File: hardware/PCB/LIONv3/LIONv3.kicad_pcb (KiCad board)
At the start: 2 copper layers, 45 x 75 mm, 67 parts, among them J1 CAN, J2 UART, J3 JTAG, J4 PWR_GND, J5 PWR_3.3V, J6 PWR_5V, J7 I2C, U1 TPS259474ARPWR, U10 XL-1608UBC-04, U11 XL-1608UBC-04, U12 TYPE-C_16PIN_2MD(073), U14 E80-900M2213S, U2 ESP32-C6-MINI-1-N4, U3 XL-1608UGC-04, U4 TLV75533PDQNR, U5 TCAN3414DR, U6 TMP112AIDRLR, U7 INA226AIDGSR, U8 XL-1608SURC-06, U9 INA226AIDGSR

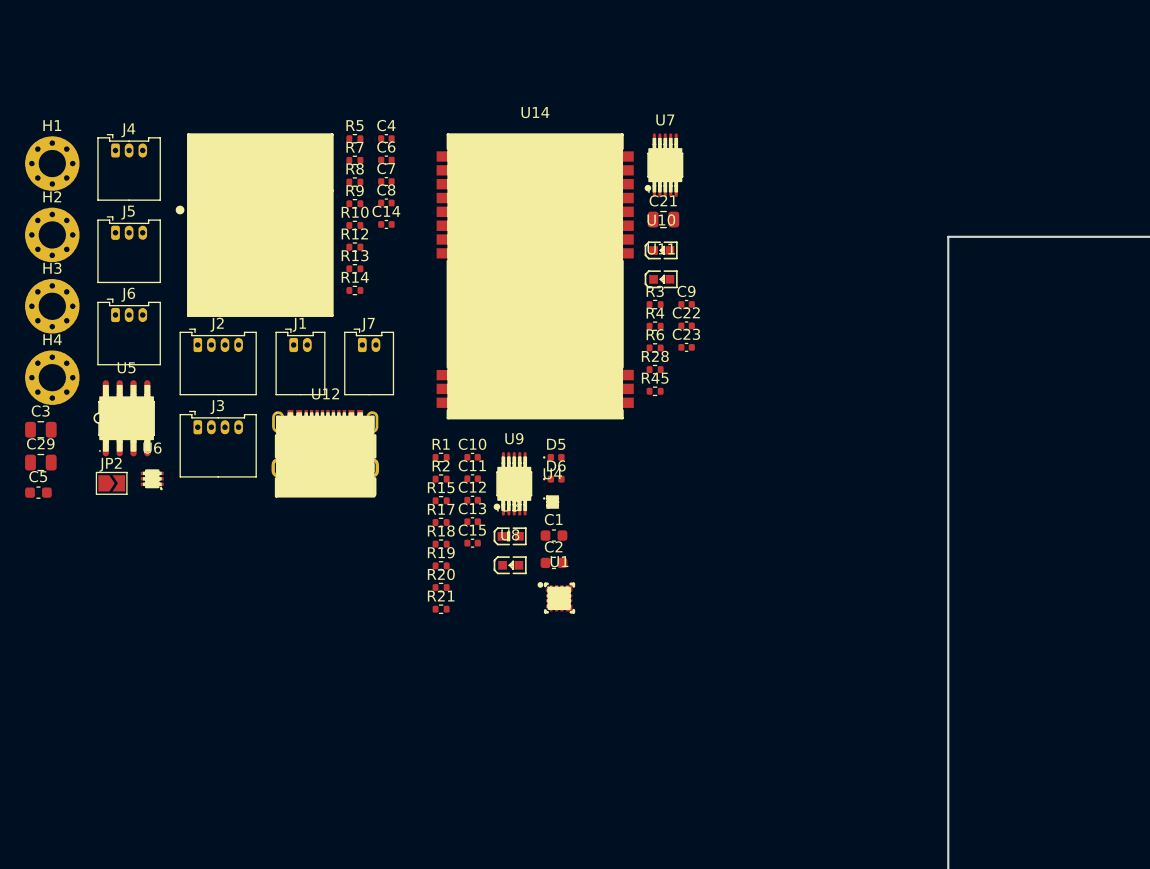
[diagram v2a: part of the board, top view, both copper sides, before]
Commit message: feat(hardware): add MOLEX connectors
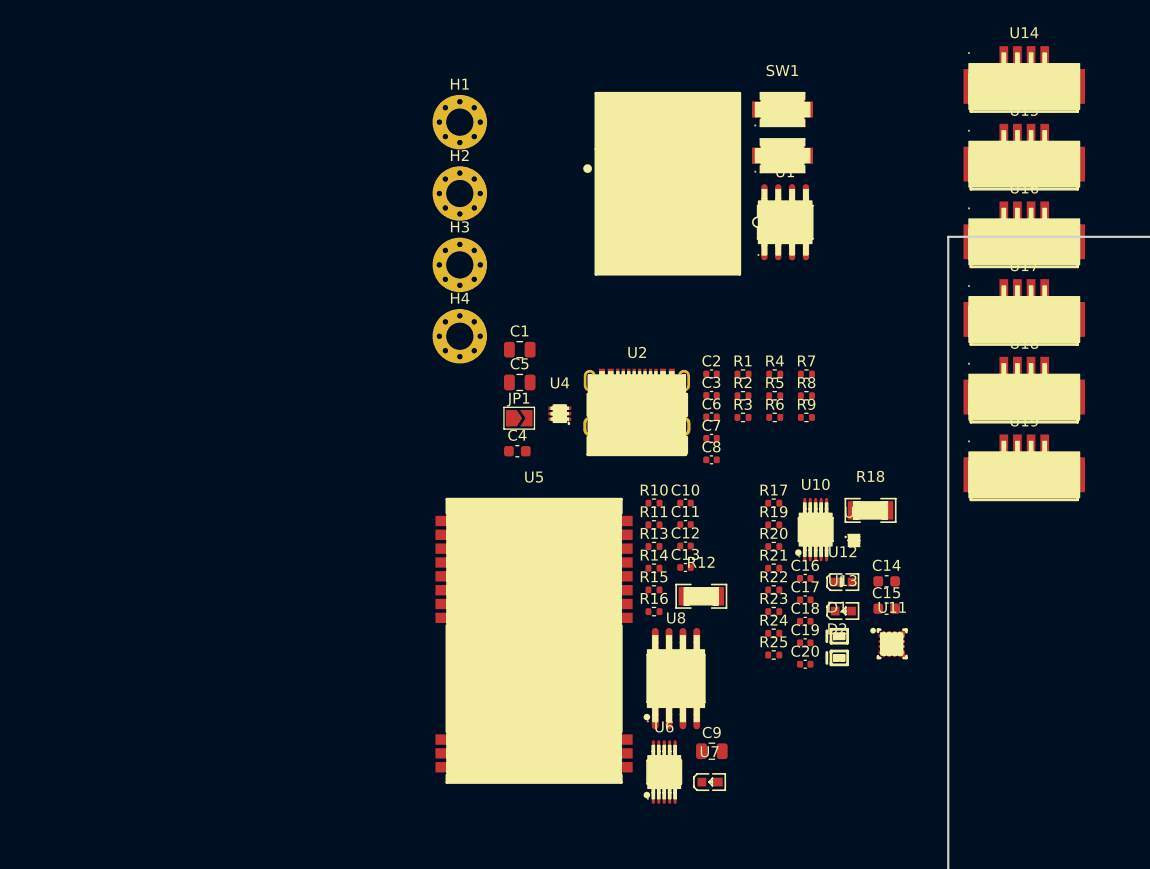
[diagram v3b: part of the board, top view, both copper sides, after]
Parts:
- removed C21: 22uF, Capacitor_SMD:C_0805_2012Metric
- removed C22, C23: 100nF, Capacitor_SMD:C_0402_1005Metric
- removed C29: 10uF, Capacitor_SMD:C_0805_2012Metric
- removed D5, D6: D_Schottky, Diode_SMD:D_0402_1005Metric
- removed J1: CAN, Connector_Molex:Molex_PicoBlade_53048-0210_1x02_P1.25mm_Horizontal
- removed J2: UART, Connector_Molex:Molex_PicoBlade_53048-0410_1x04_P1.25mm_Horizontal
- removed J3: JTAG, Connector_Molex:Molex_PicoBlade_53048-0410_1x04_P1.25mm_Horizontal
- removed J4: PWR_GND, Connector_Molex:Molex_PicoBlade_53048-0310_1x03_P1.25mm_Horizontal
- removed J5: PWR_3.3V, Connector_Molex:Molex_PicoBlade_53048-0310_1x03_P1.25mm_Horizontal
- removed J6: PWR_5V, Connector_Molex:Molex_PicoBlade_53048-0310_1x03_P1.25mm_Horizontal
- removed J7: I2C, Connector_Molex:Molex_PicoBlade_53048-0210_1x02_P1.25mm_Horizontal
- removed JP2: Jumper_2_Open, Jumper:SolderJumper-2_P1.3mm_Open_TrianglePad1.0x1.5mm
- removed R28, R45: 10k, Resistor_SMD:R_0402_1005Metric
- added C16: 100nF, Capacitor_SMD:C_0402_1005Metric, F.Cu at (138.1, 96.2)
- added C17: 1uF, Capacitor_SMD:C_0402_1005Metric, F.Cu at (138.1, 98.2)
- added C18: 3.3nF, Capacitor_SMD:C_0402_1005Metric, F.Cu at (138.1, 100.2)
- added C19: 2.2nF, Capacitor_SMD:C_0402_1005Metric, F.Cu at (138.1, 102.2)
- added C20: 1uF, Capacitor_SMD:C_0402_1005Metric, F.Cu at (138.1, 104.1)
- added D1: D_Schottky, LIONv3-Footprints:X2-DFN1006-2_L1.0-W0.6-P0.65-RD, F.Cu at (141.2, 101.6)
- added D2: D_Schottky, LIONv3-Footprints:X2-DFN1006-2_L1.0-W0.6-P0.65-RD, F.Cu at (141.2, 103.5)
- added JP1: Jumper_2_Open, Jumper:SolderJumper-2_P1.3mm_Open_TrianglePad1.0x1.5mm, F.Cu at (111.8, 81.5)
- added R11: 10k, Resistor_SMD:R_0402_1005Metric, F.Cu at (124.2, 91.3)
- added R16: 10k, Resistor_SMD:R_0402_1005Metric, F.Cu at (124.2, 99.3)
- added R22: 15k, Resistor_SMD:R_0402_1005Metric, F.Cu at (135.2, 97.3)
- added R23: 10k, Resistor_SMD:R_0402_1005Metric, F.Cu at (135.2, 99.3)
- added R24: 82, Resistor_SMD:R_0402_1005Metric, F.Cu at (135.2, 101.3)
- added R25: 150, Resistor_SMD:R_0402_1005Metric, F.Cu at (135.2, 103.3)
- added SW1: RESET, LIONv3-Footprints:KEY-SMD_L3.9-W3.0-LS5.0, F.Cu at (136.0, 53.2)
- added SW2: BOOT, LIONv3-Footprints:KEY-SMD_L3.9-W3.0-LS5.0, F.Cu at (136.0, 57.5)
- added U13: XL-1608SURC-06, LIONv3-Footprints:LED0603-RD_RED, F.Cu at (141.6, 99.2)
- added U15: UART, LIONv3-Footprints:CONN-SMD_4P-P1.25_53261-0471, F.Cu at (158.2, 56.8)
- added U16: UART, LIONv3-Footprints:CONN-SMD_4P-P1.25_53261-0471, F.Cu at (158.2, 63.9)
- added U17: UART, LIONv3-Footprints:CONN-SMD_4P-P1.25_53261-0471, F.Cu at (158.2, 71.0)
- added U18: UART, LIONv3-Footprints:CONN-SMD_4P-P1.25_53261-0471, F.Cu at (158.2, 78.2)
- added U19: UART, LIONv3-Footprints:CONN-SMD_4P-P1.25_53261-0471, F.Cu at (158.2, 85.3)
- C1: value 1uF -> 10uF; footprint Capacitor_SMD:C_0603_1608Metric -> Capacitor_SMD:C_0805_2012Metric
- C11: value 1uF -> 100nF
- C12: value 3.3nF -> 100nF
- C13: value 2.2nF -> 100nF
- C14, C4: value 100nF -> 1uF; footprint Capacitor_SMD:C_0402_1005Metric -> Capacitor_SMD:C_0603_1608Metric
- C15: footprint Capacitor_SMD:C_0402_1005Metric -> Capacitor_SMD:C_0603_1608Metric
- C2: value 1uF -> 100nF; footprint Capacitor_SMD:C_0603_1608Metric -> Capacitor_SMD:C_0402_1005Metric
- C3: value 22uF -> 100nF; footprint Capacitor_SMD:C_0805_2012Metric -> Capacitor_SMD:C_0402_1005Metric
- C5: value 1uF -> 22uF; footprint Capacitor_SMD:C_0603_1608Metric -> Capacitor_SMD:C_0805_2012Metric
- C6: value 100nF -> 4.7 nF
- C8: value 4.7 nF -> 100nF
- C9: value 100nF -> 22uF; footprint Capacitor_SMD:C_0402_1005Metric -> Capacitor_SMD:C_0805_2012Metric
- R1: value 150 -> 0
- R10: value 5.1k -> 10k
- R12: value 61 -> 50m; footprint Resistor_SMD:R_0402_1005Metric -> LIONv3-Footprints:R1206
- R13: value 61 -> 10k
- R14: value 4.7k -> 68
- R17: value 133k -> 10k
- R18: value 100k -> 50m; footprint Resistor_SMD:R_0402_1005Metric -> LIONv3-Footprints:R1206
- R19: value 6.65k -> 133k
- R2: value 82 -> 62
- R20: value 15k -> 100k
- R21: value 10k -> 6.65k
- R3: value 68 -> 62
- R4: value 68 -> 10k
- R5, R6: value 10k -> 5.1k
- R7: value 0 -> 10k
- R9: value 5.1k -> 4.7k
- U1: value TPS259474ARPWR -> TCAN3414DR; footprint LIONv3-Footprints:VQFN-10_L2.0-W2.0-P0.45-TL -> LIONv3-Footprints:SOIC-8_L4.9-W3.9-P1.27-LS6.0-BL
- U10: value XL-1608UBC-04 -> INA226AIDGSR; footprint LIONv3-Footprints:LED0603-RD_BLUE -> LIONv3-Footprints:MSOP-10_L3.0-W3.0-P0.50-LS5.0-BL
- U11: value XL-1608UBC-04 -> TPS259474ARPWR; footprint LIONv3-Footprints:LED0603-RD_BLUE -> LIONv3-Footprints:VQFN-10_L2.0-W2.0-P0.45-TL
- U12: value TYPE-C_16PIN_2MD(073) -> XL-1608UGC-04; footprint LIONv3-Footprints:USB-C-SMD_TYPE-C-16PIN-2MD-073 -> LIONv3-Footprints:LED0603-RD_GREEN
- U14: value E80-900M2213S -> UART; footprint LIONv3-Footprints:WIFIM-SMD_22P-L26.0-W16.0-P1.27-TL -> LIONv3-Footprints:CONN-SMD_4P-P1.25_53261-0471
- U2: value ESP32-C6-MINI-1-N4 -> TYPE-C_16PIN_2MD(073); footprint LIONv3-Footprints:WIFIM-SMD_61P-L16.6-W13.2-P0.80-ESP32-C6-MINI-1-N4 -> LIONv3-Footprints:USB-C-SMD_TYPE-C-16PIN-2MD-073
- U3: value XL-1608UGC-04 -> ESP32-C6-MINI-1-N4; footprint LIONv3-Footprints:LED0603-RD_GREEN -> LIONv3-Footprints:WIFIM-SMD_61P-L16.6-W13.2-P0.80-ESP32-C6-MINI-1-N4
- U4: value TLV75533PDQNR -> TMP112AIDRLR; footprint LIONv3-Footprints:X2SON-4_L1.0-W1.0-P0.65-TL-EP -> LIONv3-Footprints:SOT-563_L1.6-W1.2-P0.50-LS1.6-BR
- U5: value TCAN3414DR -> E80-900M2213S; footprint LIONv3-Footprints:SOIC-8_L4.9-W3.9-P1.27-LS6.0-BL -> LIONv3-Footprints:WIFIM-SMD_22P-L26.0-W16.0-P1.27-TL
- U6: value TMP112AIDRLR -> INA226AIDGSR; footprint LIONv3-Footprints:SOT-563_L1.6-W1.2-P0.50-LS1.6-BR -> LIONv3-Footprints:MSOP-10_L3.0-W3.0-P0.50-LS5.0-BL
- U7: value INA226AIDGSR -> XL-1608UBC-04; footprint LIONv3-Footprints:MSOP-10_L3.0-W3.0-P0.50-LS5.0-BL -> LIONv3-Footprints:LED0603-RD_BLUE
- U8: value XL-1608SURC-06 -> W25Q16JVSSIQTR; footprint LIONv3-Footprints:LED0603-RD_RED -> LIONv3-Footprints:SOIC-8_L5.3-W5.3-P1.27-LS8.0-BL
- U9: value INA226AIDGSR -> TLV75533PDQNR; footprint LIONv3-Footprints:MSOP-10_L3.0-W3.0-P0.50-LS5.0-BL -> LIONv3-Footprints:X2SON-4_L1.0-W1.0-P0.65-TL-EP
- moved C3 61.6 mm to (129.5, 79.5)
- moved U7 56.8 mm to (129.3, 114.9)
- moved C14 56.4 mm to (145.5, 96.5)
- moved U6 54.1 mm to (125.1, 114.0)
- moved U12 49.3 mm to (141.6, 96.6)
- moved U14 48.8 mm to (158.2, 49.7)
- moved R7 45.8 mm to (138.2, 77.5)
- moved R8 45.8 mm to (138.2, 79.5)
- moved R9 45.8 mm to (138.2, 81.5)
- moved C5 45.3 mm to (111.9, 78.3)
- moved R5 45.2 mm to (135.3, 79.5)
- moved R12 45.1 mm to (128.5, 97.9)
- moved U5 42.8 mm to (113.2, 102.3)
- moved C9 41.1 mm to (129.5, 112.1)
- moved U1 40.3 mm to (136.2, 63.6)
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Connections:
- C1 pad 1: Net-(D5-K) -> +3.3V
- C10 pad 1: Net-(U9-VS+) -> 3.3V_RF
- C11 pad 1: /POWER/3V3_IN -> /LR_RST
- C12 pad 1: Net-(U1-ITIMER) -> +3.3V
- C13 pad 1: Net-(U1-DVDT) -> +3.3V
- C14 pad 1: +3.3V -> Net-(D1-K)
- C15 pad 1: +3.3V -> /POWER/PWR
- C2 pad 1: /POWER/3V3_IN -> +3.3V
- C3 pad 1: +3V3 -> Net-(C3-Pad1)
- C4 pad 1: +3V3 -> Net-(U3-EN)
- C5 pad 1: Net-(U2-EN) -> +3.3V
- C6 pad 1: +3.3V -> Net-(C6-Pad1)
- C7 pad 1: Net-(C7-Pad1) -> +3.3V
- C8 pad 1: Net-(C8-Pad1) -> +3.3V
- C9 pad 1: +3.3V -> 3.3V_RF
- R1 pad 1: Net-(U8-A) -> Net-(C3-Pad1)
- R1 pad 2: /POWER/3V3_IN -> Net-(U3-EN)
- R10 pad 1: Net-(U12-CC2) -> 3.3V_RF
- R10 pad 2: GND -> /LR_NSS
- R12 pad 1: Net-(JP2-B) -> +3.3V
- R12 pad 2: Net-(C8-Pad1) -> 3.3V_RF
- R13 pad 1: Net-(C8-Pad1) -> +3.3V
- R13 pad 2: /CAN_A_N -> /FLASH_CS
- R14 pad 1: +3.3V -> Net-(U7-A)
- R14 pad 2: /TMP_ALERT -> /LR_LED
- R15 pad 1: /POWER/PWR_INA_ALERT -> +3.3V
- R15 pad 2: +3.3V -> Net-(U8-IO3)
- R17 pad 1: /POWER/3V3_IN -> /INA_ALERT
- R17 pad 2: Net-(U1-EN/UVLO) -> +3.3V
- R18 pad 1: Net-(U1-EN/UVLO) -> /POWER/PWR
- R18 pad 2: GND -> /POWER/3V3_IN
- R19 pad 1: Net-(U1-ILM) -> /POWER/3V3_IN
- R19 pad 2: GND -> Net-(U11-EN/UVLO)
- R2 pad 1: Net-(U3-A) -> Net-(JP1-B)
- R2 pad 2: +3.3V -> Net-(C6-Pad1)
- R20 pad 1: +3.3V -> Net-(U11-EN/UVLO)
- R20 pad 2: Net-(U1-FLT#/PGTH) -> GND
- R21 pad 1: Net-(U1-FLT#/PGTH) -> Net-(U11-ILM)
- R3 pad 1: Net-(U10-A) -> Net-(C6-Pad1)
- R3 pad 2: /LR_LED_TX -> /CAN_A_N
- R4 pad 1: Net-(U11-A) -> +3.3V
- R4 pad 2: /LR_LED_RX -> Net-(U3-EN)
- R5 pad 1: +3V3 -> Net-(U2-CC1)
- R5 pad 2: Net-(U2-EN) -> GND
- R6 pad 1: /INA_ALERT -> Net-(U2-CC2)
- R6 pad 2: +3.3V -> GND
- R7 pad 1: Net-(C7-Pad1) -> +3.3V
- R7 pad 2: Net-(U2-EN) -> /IO9
- R9 pad 1: Net-(U12-CC1) -> +3.3V
- R9 pad 2: GND -> /TMP_ALERT
- U1 pad 1: Net-(U1-EN/UVLO) -> /CAN_TX
- U1 pad 3: /POWER/LED_FAULT -> +3.3V
- U1 pad 4: Net-(U1-FLT#/PGTH) -> /CAN_RX
- U1 pad 5: /POWER/3V3_IN -> GND
- U1 pad 6: +3.3V -> /CAN_A_N
- U1 pad 7: Net-(U1-DVDT) -> /CAN_A_P
- U1 pad 8: GND -> /CAN_STB
- U10 pad 2: Net-(U10-A) -> /I2C_SDA
- U11 pad 1: GND -> Net-(U11-EN/UVLO)
- U11 pad 2: Net-(U11-A) -> GND
- U14 pad 1: GND -> +3.3V
- U14 pad 2: unconnected-(U14-NC-Pad2) -> /UART_TX0
- U14 pad 3: /SPI_MISO -> /UART_RX0
- U14 pad 4: /SPI_MOSI -> GND
- U14 pad 5: /SPI_SCK -> GND
- U14 pad 6: /LR_NSS -> GND
- U2 pad 13: unconnected-(U2-IO1-Pad13) -> GND
- U3 pad 2: Net-(U3-A) -> GND
- U4 pad 1: /POWER/3V3_IN -> /I2C_SCL
- U4 pad 3: Net-(D5-K) -> /TMP_ALERT
- U4 pad 4: Net-(D5-K) -> GND
- U4 pad 5: GND -> +3.3V
- U5 pad 1: /CAN1_TX -> GND
- U5 pad 2: GND -> unconnected-(U5-NC-Pad2)
- U5 pad 3: +3.3V -> /SPI_MISO
- U5 pad 4: /CAN1_RX -> /SPI_MOSI
- U5 pad 5: GND -> /SPI_SCK
- U5 pad 6: /CAN_A_N -> /LR_NSS
- U5 pad 7: /CAN_A_P -> /LR_BUSY
- U5 pad 8: /CAN1_STB -> GND
- U6 pad 1: /SCL -> GND
- U6 pad 3: /TMP_ALERT -> unconnected-(U6-Alert-Pad3)
- U6 pad 4: GND -> /I2C_SDA
- U6 pad 5: +3.3V -> /I2C_SCL
- U6 pad 6: /SDA -> +3.3V
- U7 pad 2: GND -> Net-(U7-A)
- U8 pad 1: /POWER/LED_FAULT -> /FLASH_CS
- U8 pad 2: Net-(U8-A) -> /SPI_MISO
- U9 pad 1: GND -> /POWER/PWR
- U9 pad 3: /POWER/PWR_INA_ALERT -> Net-(D1-K)
- U9 pad 4: /POWER/I2C1_SDA -> Net-(D1-K)
- U9 pad 5: /POWER/I2C1_SCL -> GND

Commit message: feat(hardware): finish board schematic
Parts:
- removed D2: D_Schottky, LIONv3-Footprints:X2-DFN1006-2_L1.0-W0.6-P0.65-RD
- removed U9: TLV75533PDQNR, LIONv3-Footprints:X2SON-4_L1.0-W1.0-P0.65-TL-EP
- added C21: 2.2uF, Capacitor_SMD:C_0603_1608Metric, F.Cu at (130.8, 130.0)
- added C22: 2.2uF, Capacitor_SMD:C_0603_1608Metric, F.Cu at (130.8, 132.5)
- added D3: D_Schottky, LIONv3-Footprints:X2-DFN1006-2_L1.0-W0.6-P0.65-RD, F.Cu at (127.3, 130.0)
- added D4: D_Schottky, LIONv3-Footprints:X2-DFN1006-2_L1.0-W0.6-P0.65-RD, F.Cu at (127.3, 132.5)
- added R26: 4.7k, Resistor_SMD:R_0402_1005Metric, F.Cu at (136.4, 129.7)
- added R27: 4.7k, Resistor_SMD:R_0402_1005Metric, F.Cu at (136.4, 131.7)
- added R28: 0, Resistor_SMD:R_0402_1005Metric, F.Cu at (136.4, 133.7)
- added R29: 0, Resistor_SMD:R_0402_1005Metric, F.Cu at (136.4, 135.7)
- added R30: 20k, Resistor_SMD:R_0402_1005Metric, F.Cu at (127.0, 134.7)
- added R31: 10k, Resistor_SMD:R_0402_1005Metric, F.Cu at (127.0, 136.7)
- added U20: TLV76733DRVR, LIONv3-Footprints:WSON-6_L2.0-W2.0-P0.65-TL-EP, F.Cu at (131.1, 135.4)
- C14, C15: value 1uF -> TBD; footprint Capacitor_SMD:C_0603_1608Metric -> Capacitor_SMD:C_0402_1005Metric
- C6: value 4.7 nF -> 4.7nF
- D1: value D_Schottky -> TI ESD752DBZR; footprint LIONv3-Footprints:X2-DFN1006-2_L1.0-W0.6-P0.65-RD -> Package_TO_SOT_SMD:SOT-23-3
- R2, R3: value 62 -> 59
- R21: value 6.65k -> 3.32k
- U14, U2: moved to B.Cu
- U15: value UART -> I2C; moved to B.Cu
- U16: value UART -> CAN; moved to B.Cu
- U17: value UART -> PWR_3V3; moved to B.Cu
- U18: value UART -> PWR_5V; moved to B.Cu
- U19: value UART -> PWR_GND; moved to B.Cu
- moved H1 94.5 mm to (193.3, 91.4)
- moved H2 87.1 mm to (193.2, 68.2)
- moved U2 70.2 mm to (192.7, 76.4), turned to -90 degrees
- moved U6 68.3 mm to (189.5, 91.2), turned to 90 degrees
- moved U3 64.5 mm to (189.4, 71.5)
- moved U8 54.8 mm to (178.8, 90.2), turned to 90 degrees
- moved U5 54.4 mm to (162.8, 80.0)
- moved U1 52.6 mm to (185.7, 81.4)
- moved SW2 52.0 mm to (179.6, 85.8)
- moved U14 51.4 mm to (192.2, 88.2), turned to -90 degrees
- moved H4 50.9 mm to (154.7, 90.0)
- moved SW1 49.9 mm to (177.4, 81.0)
- moved H3 48.1 mm to (154.5, 68.7)
- moved U10 41.4 mm to (177.1, 75.6), turned to 90 degrees
- moved U15 31.4 mm to (187.2, 68.8)
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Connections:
- C14 pad 1: Net-(D1-K) -> /USB_D+
- C15 pad 1: /POWER/PWR -> /USB_D-
- C16 pad 1: +3.3V -> /POWER/PWR
- D1 pad 1: Net-(D1-K) -> /CAN_STB
- D1 pad 2: +5V -> /CAN_A_N
- R17 pad 2: +3.3V -> /POWER/PWR
- U10 pad 6: +3.3V -> /POWER/PWR
- U11 pad 2: GND -> Net-(U11-OVLO/OVCSEL)
- U3 pad 17: /USB_D- -> Net-(U3-IO12)
- U3 pad 18: /USB_D+ -> Net-(U3-IO13)
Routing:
- net (no net): vias 0 -> 55

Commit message: feat(hardware): add TPS259474ARPWR PCB circuit
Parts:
- removed R30: 20k, Resistor_SMD:R_0402_1005Metric
- removed R31: 10k, Resistor_SMD:R_0402_1005Metric
- added R32: 34.8k, Resistor_SMD:R_0402_1005Metric, F.Cu at (176.4, 88.0)
- R19: value 133k -> 60.4k
- R20: value 100k -> 10k
- U14, U15, U16, U17, U18, U19, U2: moved to F.Cu
- moved JP1 284.4 mm to (381.4, 172.3)
- moved C1 281.6 mm to (370.6, 186.6)
- moved C2 267.9 mm to (378.5, 176.1)
- moved C6 267.9 mm to (378.5, 180.0)
- moved R2 257.1 mm to (369.8, 178.1)
- moved R3 257.1 mm to (369.8, 180.1)
- moved U3 256.2 mm to (-56.7, 0.55)
- moved D1 249.7 mm to (381.8, 168.3)
- moved SW2 243.3 mm to (-46.2, -4.70)
- moved SW1 241.0 mm to (-46.2, -8.93)
- moved U6 229.5 mm to (-40.0, 90.3), turned to 0 degrees
- moved U10 227.0 mm to (-37.5, 149.6), turned to 0 degrees
- moved R27 220.0 mm to (-51.2, 16.8)
- moved R28 220.0 mm to (-51.2, 18.8)
- moved R29 220.0 mm to (-51.2, 20.8)
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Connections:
- net Net-(D3-K) renamed /POWER/5V_D
- R20 pad 2: GND -> Net-(U11-OVLO/OVCSEL)
- U5 pad 12: /RF/ANT_2.4 -> unconnected-(U5-ANT-Pad12)
- U5 pad 15: unconnected-(U5-ANT-Pad15) -> /RF/ANT_915
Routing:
- net GND: track 0.00 -> 6.22 mm, vias 0 -> 11
- net 3.3V_RF: track 0.00 -> 4.07 mm
- net Net-(U11-OVLO/OVCSEL): track 0.00 -> 3.63 mm
- net /LR_RST: track 0.00 -> 3.20 mm
- net Net-(U11-EN/UVLO): track 0.00 -> 3.04 mm
- net Net-(U11-FLT#/PGTH): track 0.00 -> 2.98 mm
- net Net-(U11-ITIMER): track 0.00 -> 1.80 mm
- net Net-(U11-ILM): track 0.00 -> 1.59 mm
- net Net-(U11-DVDT): track 0.00 -> 1.50 mm
- net /POWER/3V3_IN: vias 0 -> 19
- net +3.3V: vias 0 -> 20
- net (no net): vias 55 -> 0
- added copper zone on F.Cu, net +3.3V
- added copper zone on F.Cu, net /POWER/3V3_IN
- added copper zone on F.Cu, net GND

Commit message: feat(hardware): add TLV76733DRVR circuit
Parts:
- moved U4 179.3 mm to (170.8, 87.2), turned to 180 degrees
- moved C8 173.5 mm to (172.8, 87.7), turned to -90 degrees
- moved R9 173.4 mm to (168.8, 87.2), turned to -90 degrees
- moved C22 94.6 mm to (173.1, 74.7), turned to -90 degrees
- moved D4 92.4 mm to (175.8, 72.2), turned to 180 degrees
- moved D3 89.7 mm to (178.5, 70.2), turned to 90 degrees
- moved C21 89.3 mm to (178.5, 73.7), turned to -90 degrees
- moved U20 79.5 mm to (175.8, 74.5)
- moved R18 15.9 mm to (-25.9, 148.7), turned to -90 degrees
- moved R22 14.1 mm to (189.2, 76.7)
- moved C19 14.1 mm to (189.2, 74.4)
- moved R23 14.1 mm to (189.2, 79.0)
- moved U11 14.1 mm to (186.8, 75.8)
- moved C17 14.1 mm to (184.8, 75.5)
- moved C18 14.1 mm to (185.5, 72.8)
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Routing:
- net +3.3V: track 0.00 -> 2.28 mm, vias 20 -> 21
- net /TMP_ALERT: track 0.00 -> 1.30 mm
- net /POWER/5V_D: track 0.00 -> 0.97 mm, vias 0 -> 8
- net GND: vias 11 -> 20
- net /POWER/PWR: vias 0 -> 13
- added copper zone on F.Cu, net /POWER/5V_D
- added copper zone on F.Cu, net /POWER/PWR

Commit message: feat(hardware): PCB macro placement
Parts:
- removed H1, H2, H3, H4: M2.5, MountingHole:MountingHole_2.5mm_Pad_Via
- C1, C2, C6, D1, JP1, R2, R3, U1, U14, U15, U16, U17, U18, U19: moved to B.Cu
- moved D1 314.0 mm to (94.2, 42.3), turned to 90 degrees
- moved C16 297.8 mm to (263.3, 86.4)
- moved R17 297.8 mm to (255.3, 85.2)
- moved R18 297.8 mm to (265.0, 84.9)
- moved U10 297.8 mm to (259.5, 85.7)
- moved U6 282.4 mm to (235.8, 29.6), turned to -90 degrees
- moved R12 282.0 mm to (241.7, 28.8), turned to -90 degrees
- moved C12 280.5 mm to (239.7, 30.3), turned to 90 degrees
- moved U3 233.5 mm to (166.4, 69.4)
- moved SW2 233.3 mm to (170.3, 82.2)
- moved R7 232.0 mm to (170.6, 76.6), turned to 90 degrees
- moved R8 230.3 mm to (169.3, 76.6), turned to 90 degrees
- moved SW1 227.8 mm to (162.5, 82.2), turned to 180 degrees
- moved R28 225.7 mm to (166.6, 77.8), turned to -90 degrees
- moved R29 223.9 mm to (165.3, 77.8), turned to -90 degrees
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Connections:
- D1 pad 1: /CAN_STB -> /CAN_A_P
- U16 pad 1: /CAN_A_P -> unconnected-(U16-Pad1)
- U16 pad 2: unconnected-(U16-Pad2) -> /CAN_A_P
- U16 pad 3: unconnected-(U16-Pad3) -> /CAN_A_N
- U16 pad 4: /CAN_A_N -> unconnected-(U16-Pad4)
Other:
- board size 45 x 75 mm -> 45 x 80 mm
- copper layers 2 -> 4
- board text added: "FAULT"
- board text added: "ON"
- board text added: "RX/TX"
